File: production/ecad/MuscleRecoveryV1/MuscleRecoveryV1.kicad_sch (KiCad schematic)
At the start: 17 parts, among them J3 Screw_Terminal_01x06, U4 ESP32-WROOM-32

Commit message: rev1 first draft ready for review
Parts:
- added R34: 0, symbol Device:R
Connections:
- net TFT_RST: now also R34.1; no longer U4.26 (IO4)
- new net: R34.2, U4.26 (IO4)
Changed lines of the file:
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@@
-    (stroke (width 0) (type default))
-  )
-  (wire (pts (xy 157.48 71.12) (xy 165.1 71.12))
     (stroke (width 0) (type default))
   )
@@
     (stroke (width 0) (type default))
   )
+  (wire (pts (xy 157.48 71.12) (xy 160.02 71.12))
+    (stroke (width 0) (type default))
+  )
   (wire (pts (xy 86.995 173.355) (xy 96.52 173.355))
     (stroke (width 0) (type default))
@@
     (stroke (width 0) (type default))
   )
+  (wire (pts (xy 167.64 71.12) (xy 170.18 71.12))
+    (stroke (width 0) (type default))
+  )
   (wire (pts (xy 146.685 169.545) (xy 146.685 173.355))
     (stroke (width 0) (type default))
@@
     )
   )
-  (global_label "TFT_RST" (shape output) (at 165.1 71.12 0) (fields_autoplaced)
-    (effects (font (size 1.27 1.27)) (justify left))
-    (property "Intersheetrefs" "${INTERSHEET_REFS}" (at 175.5237 71.12 0)
+  (global_label "TFT_RST" (shape output) (at 170.18 71.12 0) (fields_autoplaced)
+    (effects (font (size 1.27 1.27)) (justify left))
+    (property "Intersheetrefs" "${INTERSHEET_REFS}" (at 180.6037 71.12 0)
       (effects (font (size 1.27 1.27)) (justify left) hide)
     )
@@
         )
       )
+    )
+  )
+  (symbol (lib_id "Device:R") (at 163.83 71.12 270) (unit 1)
+    (in_bom yes) (on_board yes) (dnp no)
+    (property "Reference" "R34" (at 164.465 73.025 90)
+      (effects (font (size 1.27 1.27)))
+    )
+    (property "Value" "0" (at 164.465 75.565 90)
+      (effects (font (size 1.27 1.27)))
+    )
+    (property "Footprint" "" (at 163.83 69.342 90)
+      (effects (font (size 1.27 1.27)) hide)
+    )
+    (property "Datasheet" "~" (at 163.83 71.12 0)
+      (effects (font (size 1.27 1.27)) hide)
+    )
+    (pin "1")
+    (pin "2")
+    (instances
+      (project "MuscleRecoveryV1"
+        (path "/4e550305-79d2-4e4a-a502-817ebcc79f9a"
+          (reference "R34") (unit 1)
+        )
+      )

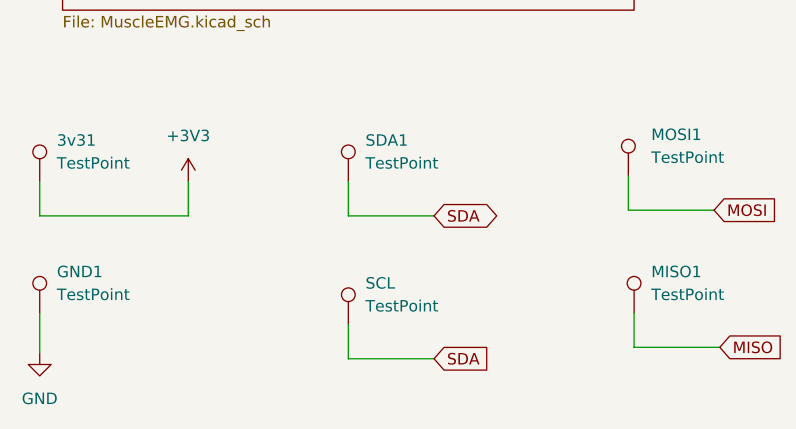
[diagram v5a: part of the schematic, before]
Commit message: Footprints added
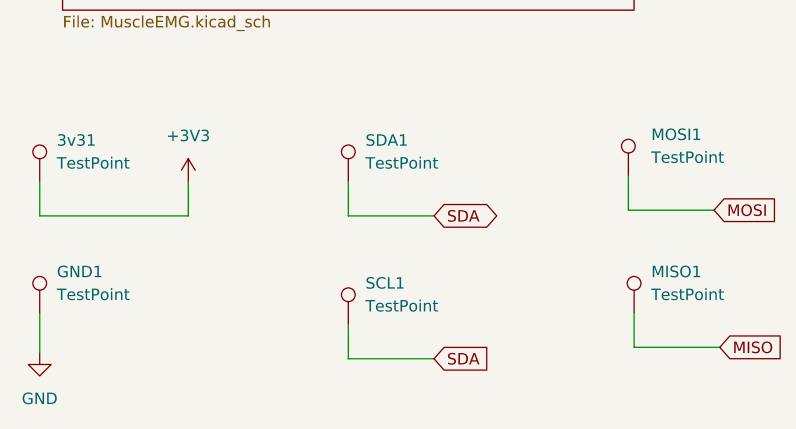
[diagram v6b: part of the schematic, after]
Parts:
- 3v31, GND1, MISO1, MOSI1, SDA1, SD_CS1, TFT_CLK1, TFT_CS1, TFT_DC1, TFT_RST1: footprint (none) -> TestPoint:TestPoint_Pad_D1.5mm
- C12, C13: footprint (none) -> Capacitor_SMD:C_0805_2012Metric
- R30, R31, R34: footprint (none) -> Resistor_SMD:R_0805_2012Metric
- SCL1: renamed from SCL; footprint (none) -> TestPoint:TestPoint_Pad_D1.5mm
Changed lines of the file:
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@@
       (effects (font (size 1.27 1.27)) (justify left))
     )
-    (property "Footprint" "" (at 151.765 169.545 0)
+    (property "Footprint" "TestPoint:TestPoint_Pad_D1.5mm" (at 151.765 169.545 0)
       (effects (font (size 1.27 1.27)) hide)
     )
@@
       (effects (font (size 1.27 1.27)) (justify left))
     )
-    (property "Footprint" "" (at 26.67 170.18 0)
+    (property "Footprint" "TestPoint:TestPoint_Pad_D1.5mm" (at 26.67 170.18 0)
       (effects (font (size 1.27 1.27)) hide)
     )
@@
       (effects (font (size 1.27 1.27)) (justify left))
     )
-    (property "Footprint" "" (at 92.71 184.785 0)
+    (property "Footprint" "TestPoint:TestPoint_Pad_D1.5mm" (at 92.71 184.785 0)
       (effects (font (size 1.27 1.27)) hide)
     )
@@
       (effects (font (size 1.27 1.27)) (justify left))
     )
-    (property "Footprint" "" (at 97.79 66.04 0)
+    (property "Footprint" "Capacitor_SMD:C_0805_2012Metric" (at 97.79 66.04 0)
       (effects (font (size 1.27 1.27)) hide)
     )
@@
       (effects (font (size 1.27 1.27)) (justify left))
     )
-    (property "Footprint" "" (at 107.95 66.04 0)
+    (property "Footprint" "Capacitor_SMD:C_0805_2012Metric" (at 107.95 66.04 0)
       (effects (font (size 1.27 1.27)) hide)
     )
@@
       (effects (font (size 1.27 1.27)) (justify left))
     )
-    (property "Footprint" "" (at 151.765 154.305 0)
+    (property "Footprint" "TestPoint:TestPoint_Pad_D1.5mm" (at 151.765 154.305 0)
       (effects (font (size 1.27 1.27)) hide)
     )
@@
       (effects (font (size 1.27 1.27)) (justify left))
     )
-    (property "Footprint" "" (at 152.4 184.15 0)
+    (property "Footprint" "TestPoint:TestPoint_Pad_D1.5mm" (at 152.4 184.15 0)
       (effects (font (size 1.27 1.27)) hide)
     )
@@
       (effects (font (size 1.27 1.27)) (justify left))
     )
-    (property "Footprint" "" (at 184.912 91.44 90)
+    (property "Footprint" "Resistor_SMD:R_0805_2012Metric" (at 184.912 91.44 90)
       (effects (font (size 1.27 1.27)) hide)
     )
@@
   (symbol (lib_id "Connector:TestPoint") (at 55.88 186.055 0) (unit 1)
     (in_bom yes) (on_board yes) (dnp no) (fields_autoplaced)
-    (property "Reference" "SCL" (at 57.785 181.483 0)
+    (property "Reference" "SCL1" (at 57.785 181.483 0)
       (effects (font (size 1.27 1.27)) (justify left))
     )
@@
       (effects (font (size 1.27 1.27)) (justify left))
     )
-    (property "Footprint" "" (at 60.96 186.055 0)
+    (property "Footprint" "TestPoint:TestPoint_Pad_D1.5mm" (at 60.96 186.055 0)
       (effects (font (size 1.27 1.27)) hide)
     )
@@
       (project "MuscleRecoveryV1"
         (path "/4e550305-79d2-4e4a-a502-817ebcc79f9a"
-          (reference "SCL") (unit 1)
+          (reference "SCL1") (unit 1)
         )
       )
@@
       (effects (font (size 1.27 1.27)) (justify left))
     )
-    (property "Footprint" "" (at 120.015 170.18 0)
+    (property "Footprint" "TestPoint:TestPoint_Pad_D1.5mm" (at 120.015 170.18 0)
       (effects (font (size 1.27 1.27)) hide)
     )
@@
       (effects (font (size 1.27 1.27)) (justify right))
     )
-    (property "Footprint" "" (at 184.658 91.44 90)
+    (property "Footprint" "Resistor_SMD:R_0805_2012Metric" (at 184.658 91.44 90)
       (effects (font (size 1.27 1.27)) hide)
     )
@@
       (effects (font (size 1.27 1.27)) (justify left))
     )
-    (property "Footprint" "" (at 26.67 184.785 0)
+    (property "Footprint" "TestPoint:TestPoint_Pad_D1.5mm" (at 26.67 184.785 0)
       (effects (font (size 1.27 1.27)) hide)
     )
@@
       (effects (font (size 1.27 1.27)) (justify left))
     )
-    (property "Footprint" "" (at 120.65 184.785 0)
+    (property "Footprint" "TestPoint:TestPoint_Pad_D1.5mm" (at 120.65 184.785 0)
       (effects (font (size 1.27 1.27)) hide)
     )
@@
       (effects (font (size 1.27 1.27)))
     )
-    (property "Footprint" "" (at 163.83 69.342 90)
+    (property "Footprint" "Resistor_SMD:R_0805_2012Metric" (at 163.83 69.342 90)
       (effects (font (size 1.27 1.27)) hide)
     )
@@
       (effects (font (size 1.27 1.27)) (justify left))
     )
-    (property "Footprint" "" (at 92.075 169.545 0)
+    (property "Footprint" "TestPoint:TestPoint_Pad_D1.5mm" (at 92.075 169.545 0)
       (effects (font (size 1.27 1.27)) hide)
     )
@@
       (effects (font (size 1.27 1.27)) (justify left))
     )
-    (property "Footprint" "" (at 60.96 170.18 0)
-      (effects (font (size 1.27 1.27)) hide)
-    )
+    (property "Footprint" "TestPoint:TestPoint_Pad_D1.5mm" (at 60.96 170.18 0)
+      (effects (font (size 1.27 1.27)) hide)
+    )

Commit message: Maggie fixing her mistakes lol
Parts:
- removed J3: Screw_Terminal_01x06, symbol Connector:Screw_Terminal_01x06
- added J6: Screw_Terminal_01x06, symbol Connector:Screw_Terminal_01x06
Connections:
- net +3V3: now also J6.6 (Pin_6)
- net GND: now also J6.1 (Pin_1)
- net IO27: now also J6.4 (Pin_4)
- net IO32: now also J6.3 (Pin_3)
- net IO35: now also J6.2 (Pin_2)
- net IO26: now reaches U4.11 (IO26)
- net IO26: now also J6.5 (Pin_5)
- net IO34 renamed ALT_START_BUTTON
- no-connect marks 13 -> 12
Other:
- sheet Display ports: added ALT_START_BUTTON; removed none

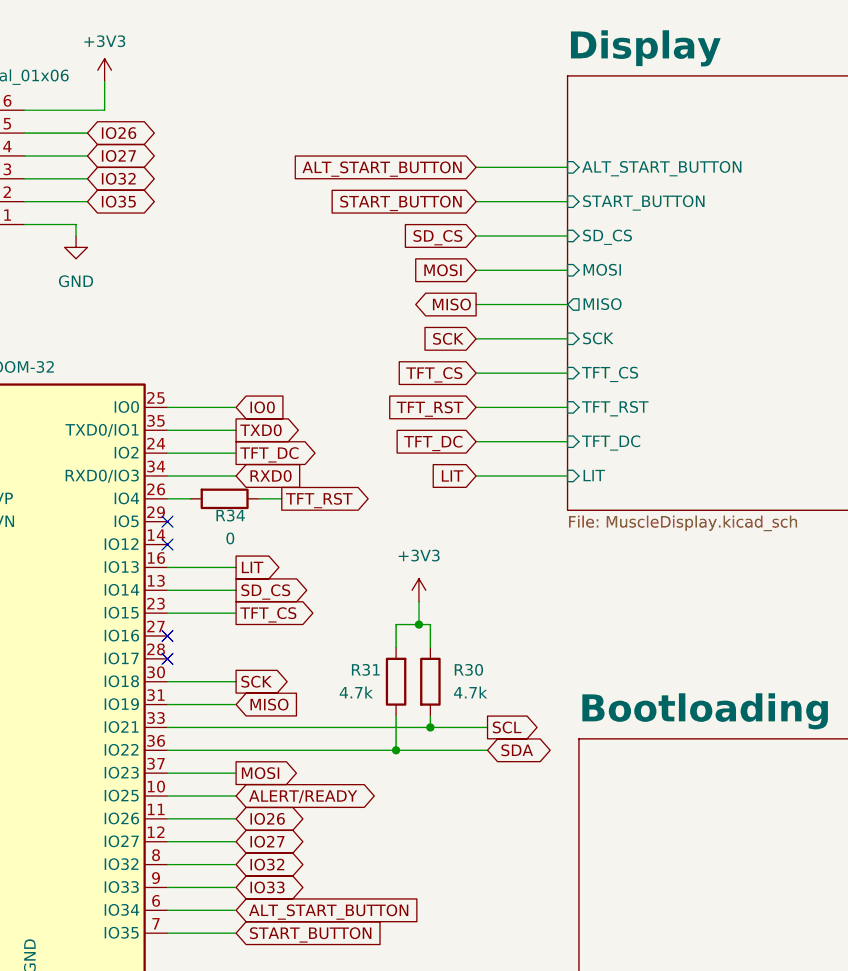
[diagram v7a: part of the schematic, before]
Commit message: Adding Motor Circuitry
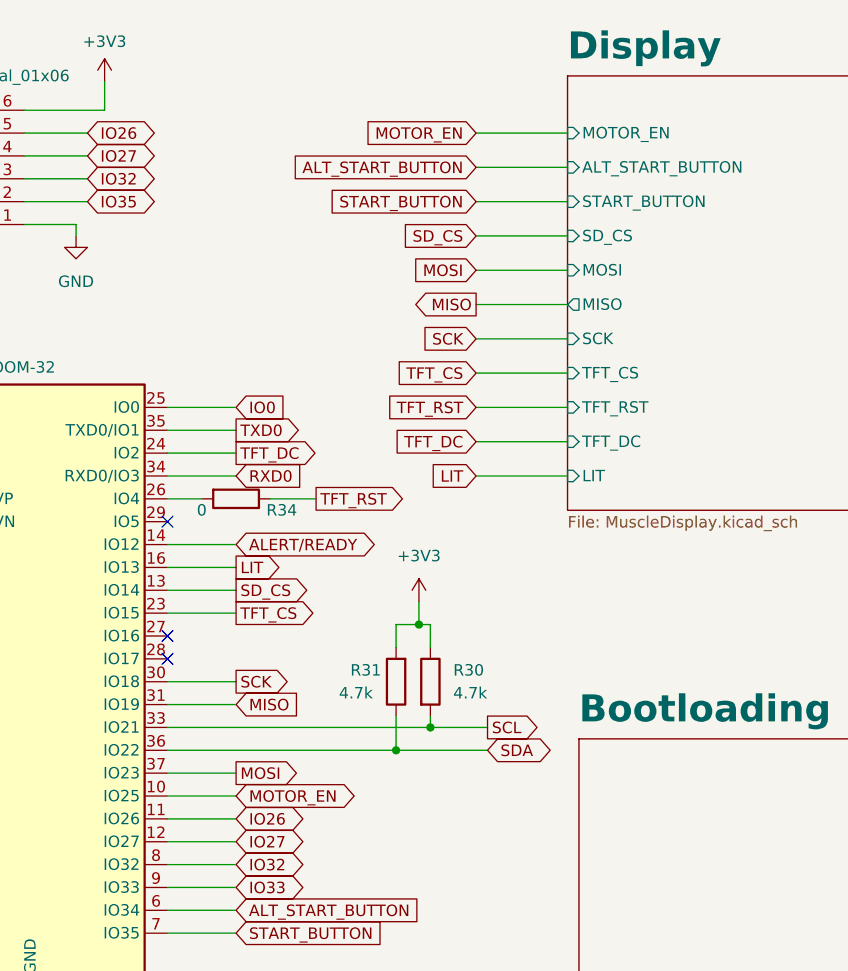
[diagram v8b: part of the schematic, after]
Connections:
- net ALERT/READY: now also U4.14 (IO12); no longer U4.10 (IO25)
- new net MOTOR_EN: U4.10 (IO25)
- no-connect marks 12 -> 11
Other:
- sheet Display ports: added MOTOR_EN; removed none
- moved on the sheet: R34
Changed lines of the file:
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@@
   (no_connect (at 127 99.06))
   (no_connect (at 157.48 88.9))
-  (no_connect (at 157.48 76.2))
   (no_connect (at 127 91.44))
   (no_connect (at 127 96.52))
@@
     (stroke (width 0) (type default))
   )
+  (wire (pts (xy 191.77 30.48) (xy 201.93 30.48))
+    (stroke (width 0) (type default))
+  )
   (wire (pts (xy 193.04 142.24) (xy 203.2 142.24))
     (stroke (width 0) (type default))
@@
     (stroke (width 0) (type default))
   )
-  (wire (pts (xy 157.48 71.12) (xy 160.02 71.12))
+  (wire (pts (xy 157.48 71.12) (xy 161.29 71.12))
     (stroke (width 0) (type default))
   )
@@
     (stroke (width 0) (type default))
   )
-  (wire (pts (xy 167.64 71.12) (xy 170.18 71.12))
+  (wire (pts (xy 168.91 71.12) (xy 173.99 71.12))
     (stroke (width 0) (type default))
   )
@@
     (stroke (width 0) (type default))
   )
+  (wire (pts (xy 157.48 76.2) (xy 165.1 76.2))
+    (stroke (width 0) (type default))
+  )
   (wire (pts (xy 86.995 169.545) (xy 86.995 173.355))
     (stroke (width 0) (type default))
@@
     )
   )
-  (global_label "TFT_RST" (shape output) (at 170.18 71.12 0) (fields_autoplaced)
-    (effects (font (size 1.27 1.27)) (justify left))
-    (property "Intersheetrefs" "${INTERSHEET_REFS}" (at 180.6037 71.12 0)
+  (global_label "MOTOR_EN" (shape bidirectional) (at 165.1 104.14 0) (fields_autoplaced)
+    (effects (font (size 1.27 1.27)) (justify left))
+    (property "Intersheetrefs" "${INTERSHEET_REFS}" (at 178.9936 104.14 0)
+      (effects (font (size 1.27 1.27)) (justify left) hide)
+    )
+  )
+  (global_label "TFT_RST" (shape output) (at 173.99 71.12 0) (fields_autoplaced)
+    (effects (font (size 1.27 1.27)) (justify left))
+    (property "Intersheetrefs" "${INTERSHEET_REFS}" (at 184.4137 71.12 0)
       (effects (font (size 1.27 1.27)) (justify left) hide)
     )
@@
     )
   )
+  (global_label "MOTOR_EN" (shape input) (at 191.77 30.48 180) (fields_autoplaced)
+    (effects (font (size 1.27 1.27)) (justify right))
+    (property "Intersheetrefs" "${INTERSHEET_REFS}" (at 178.9877 30.48 0)
+      (effects (font (size 1.27 1.27)) (justify right) hide)
+    )
+  )
   (global_label "SDA" (shape bidirectional) (at 65.405 173.99 0) (fields_autoplaced)
     (effects (font (size 1.27 1.27)) (justify left))
@@
     )
   )
-  (global_label "ALERT{slash}READY" (shape bidirectional) (at 165.1 104.14 0) (fields_autoplaced)
-    (effects (font (size 1.27 1.27)) (justify left))
-    (property "Intersheetrefs" "${INTERSHEET_REFS}" (at 181.8965 104.14 0)
-      (effects (font (size 1.27 1.27)) (justify left) hide)
-    )
-  )
   (global_label "TFT_CS" (shape input) (at 191.77 57.15 180) (fields_autoplaced)
     (effects (font (size 1.27 1.27)) (justify right))
@@
     (effects (font (size 1.27 1.27)) (justify left))
     (property "Intersheetrefs" "${INTERSHEET_REFS}" (at 173.5508 109.22 0)
+      (effects (font (size 1.27 1.27)) (justify left) hide)
+    )
+  )
+  (global_label "ALERT{slash}READY" (shape bidirectional) (at 165.1 76.2 0) (fields_autoplaced)
+    (effects (font (size 1.27 1.27)) (justify left))
+    (property "Intersheetrefs" "${INTERSHEET_REFS}" (at 181.8965 76.2 0)
       (effects (font (size 1.27 1.27)) (justify left) hide)
     )
@@
     )
   )
-  (symbol (lib_id "Device:R") (at 163.83 71.12 270) (unit 1)
+  (symbol (lib_id "Device:R") (at 165.1 71.12 270) (unit 1)
     (in_bom yes) (on_board yes) (dnp no)
-    (property "Reference" "R34" (at 164.465 73.025 90)
+    (property "Reference" "R34" (at 170.18 72.39 90)
       (effects (font (size 1.27 1.27)))
     )
-    (property "Value" "0" (at 164.465 75.565 90)
+    (property "Value" "0" (at 161.29 72.39 90)
       (effects (font (size 1.27 1.27)))
     )
-    (property "Footprint" "Resistor_SMD:R_0805_2012Metric" (at 163.83 69.342 90)
-      (effects (font (size 1.27 1.27)) hide)
-    )
-    (property "Datasheet" "~" (at 163.83 71.12 0)
+    (property "Footprint" "Resistor_SMD:R_0805_2012Metric" (at 165.1 69.342 90)
+      (effects (font (size 1.27 1.27)) hide)
+    )
+    (property "Datasheet" "~" (at 165.1 71.12 0)
       (effects (font (size 1.27 1.27)) hide)
     )
@@
       (effects (font (size 1.27 1.27)) (justify left))
     )
+    (pin "MOTOR_EN" input (at 201.93 30.48 180)
+      (effects (font (size 1.27 1.27)) (justify left))
+    )
